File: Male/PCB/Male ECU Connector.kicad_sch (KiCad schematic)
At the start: 3 parts

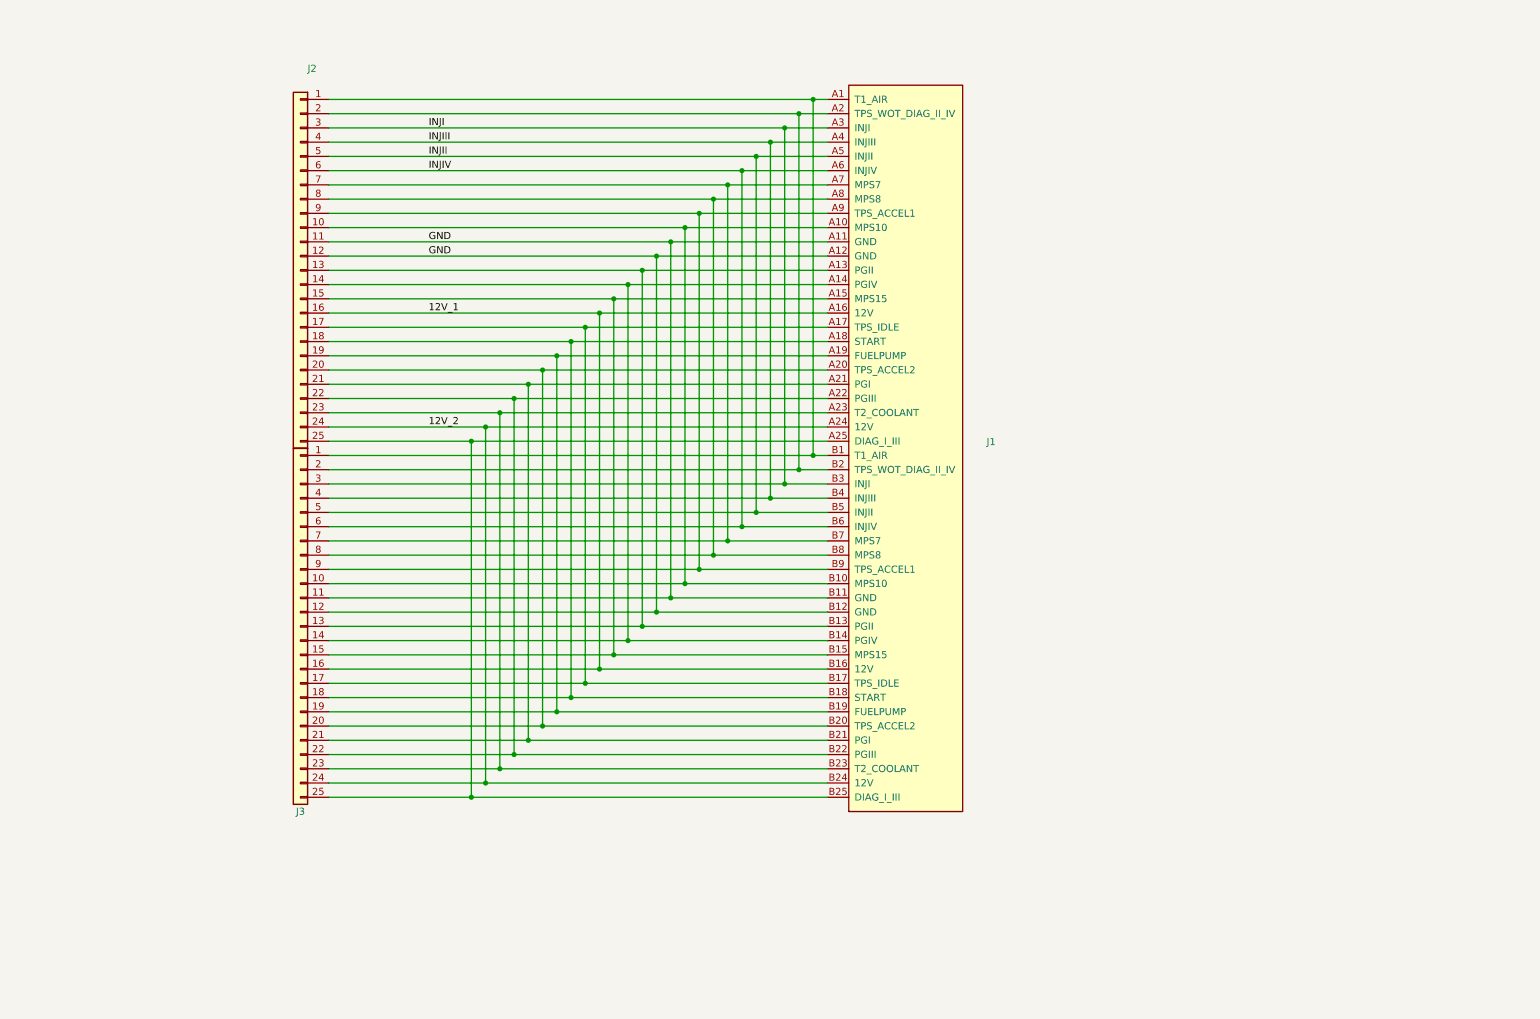
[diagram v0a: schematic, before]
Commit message: Added relay to disable fuel pump.
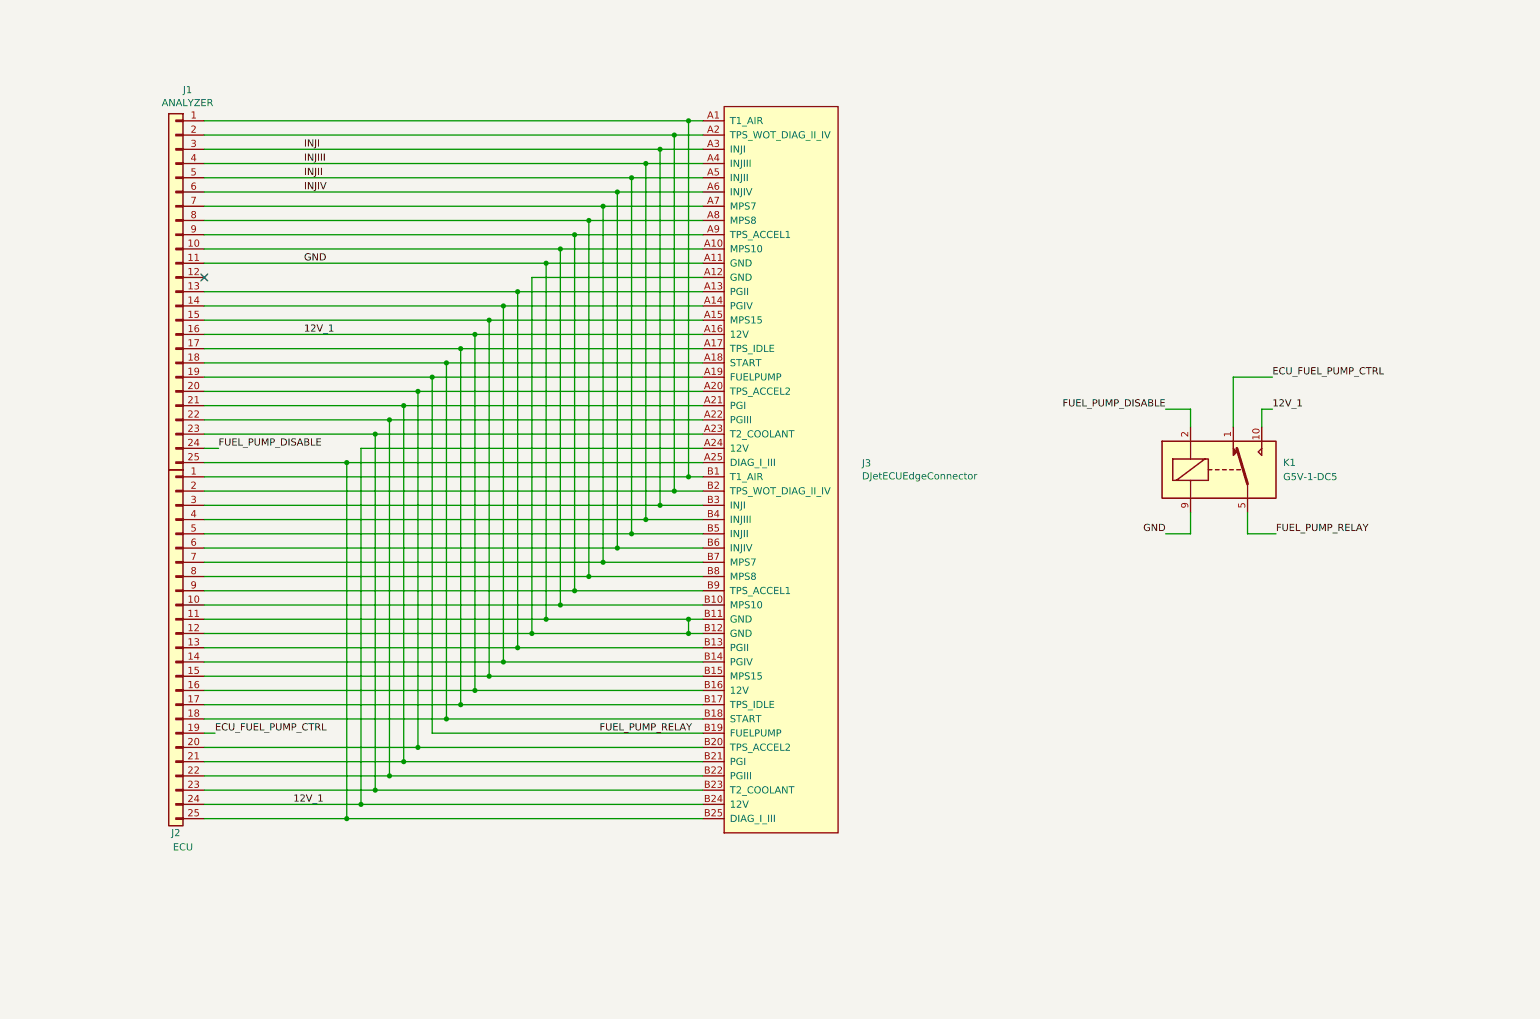
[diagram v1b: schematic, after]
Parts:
- added K1: G5V-1-DC5, Relay_THT:Relay_SPDT_Omron_G5V-1, symbol Relay:G5V-1
- J1: renamed from J2; value (none) -> ANALYZER; footprint (none) -> Connector_PinHeader_2.54mm:PinHeader_1x25_P2.54mm_Vertical
- J2: renamed from J3; value (none) -> ECU; footprint (none) -> Connector_PinHeader_2.54mm:PinHeader_1x25_P2.54mm_Vertical
- J3: renamed from J1; value (none) -> DJetECUEdgeConnector; footprint (none) -> Britishideas:D-Jetronic ECU Edge Connector
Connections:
- net 12V_1: now also J2.24 (Pin_24), J3.A24 (12V), J3.B24 (12V), K1.10
- net GND: now also K1.9; no longer J1.12 (Pin_12)
- net FUEL_PUMP_RELAY: now reaches J1.19 (Pin_19), J3.A19 (FUELPUMP), J3.B19 (FUELPUMP)
- net FUEL_PUMP_RELAY: now also K1.5, K1.6; no longer J2.19 (Pin_19)
- removed net 12V_2: J1.24 (Pin_24), J2.24 (Pin_24), J3.A24 (12V), J3.B24 (12V)
- new net ECU_FUEL_PUMP_CTRL: J2.19 (Pin_19), K1.1
- new net FUEL_PUMP_DISABLE: J1.24 (Pin_24), K1.2
- no-connect marks 0 -> 1
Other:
- moved on the sheet: J1, J2, J3

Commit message: Added larger holes for 18AWG (0.75mm2) engine harness wires. Rounded back corners of PCB to make it easier to design case. Added solder jumper to make relay optional.
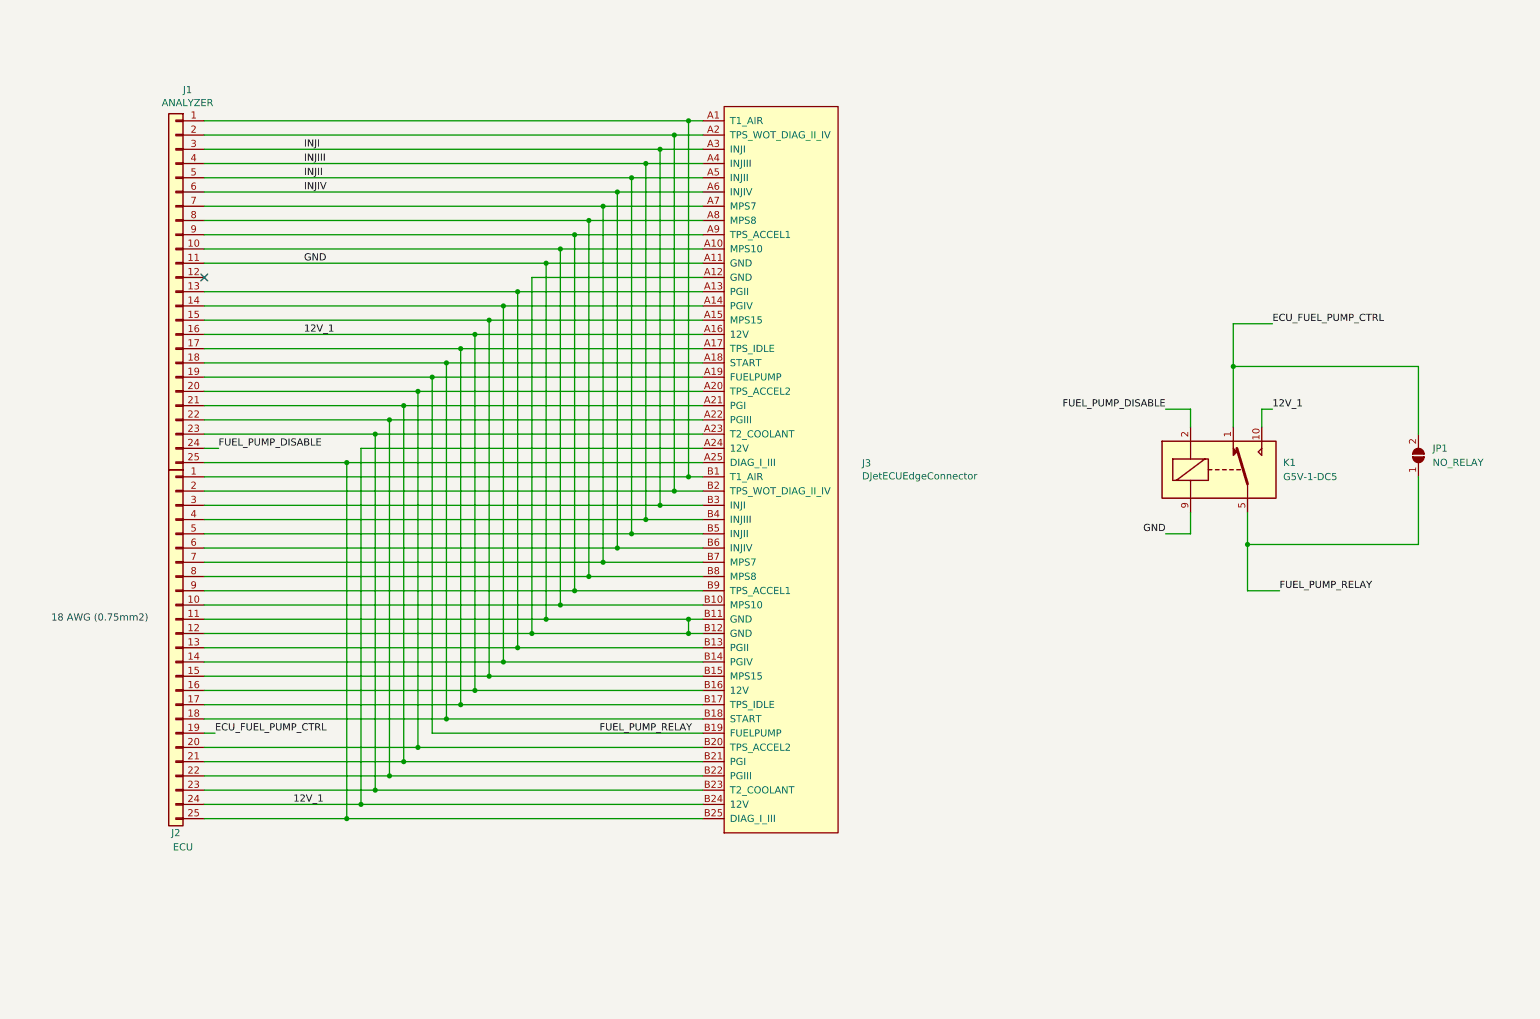
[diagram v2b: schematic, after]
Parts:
- added JP1: NO_RELAY, Jumper:SolderJumper-2_P1.3mm_Open_TrianglePad1.0x1.5mm, symbol Jumper:SolderJumper_2_Open
- J2: footprint Connector_PinHeader_2.54mm:PinHeader_1x25_P2.54mm_Vertical -> Britishideas:Pins_1x25_P3.00mm_18AWG
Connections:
- net ECU_FUEL_PUMP_CTRL: now also JP1.2 (B)
- net FUEL_PUMP_RELAY: now also JP1.1 (A)
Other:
- note added: "18 AWG (0.75mm2)"
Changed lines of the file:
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@@
   (title_block
     (title "Male ECU Connector for D-Jetronic")
-    (date "2023-10-20")
+    (date "2023-10-21")
     (rev "V1.1")
     (company "djetronic.org")
@@
   (junction (at 102.235 130.81) (diameter 0) (color 0 0 0 0)
   )
+  (junction (at 232.41 78.105) (diameter 0) (color 0 0 0 0)
+  )
   (junction (at 135.255 97.79) (diameter 0) (color 0 0 0 0)
   )
   (junction (at 97.155 135.89) (diameter 0) (color 0 0 0 0)
+  )
+  (junction (at 234.95 109.855) (diameter 0) (color 0 0 0 0)
   )
   (junction (at 109.855 59.69) (diameter 0) (color 0 0 0 0)
@@
     (stroke (width 0) (type default) (color 0 0 0 0))
   )
+  (wire (pts (xy 265.43 97.79) (xy 265.43 109.855))
+    (stroke (width 0) (type default) (color 0 0 0 0))
+  )
   (wire (pts (xy 48.895 118.11) (xy 114.935 118.11))
     (stroke (width 0) (type default) (color 0 0 0 0))
@@
     (stroke (width 0) (type default) (color 0 0 0 0))
   )
-  (wire (pts (xy 234.95 104.14) (xy 234.95 107.95))
+  (wire (pts (xy 234.95 104.14) (xy 234.95 109.855))
     (stroke (width 0) (type default) (color 0 0 0 0))
   )
@@
     (stroke (width 0) (type default) (color 0 0 0 0))
   )
+  (wire (pts (xy 265.43 78.105) (xy 232.41 78.105))
+    (stroke (width 0) (type default) (color 0 0 0 0))
+  )
   (wire (pts (xy 92.075 77.47) (xy 92.075 140.97))
     (stroke (width 0) (type default) (color 0 0 0 0))
   )
+  (wire (pts (xy 234.95 109.855) (xy 234.95 118.11))
+    (stroke (width 0) (type default) (color 0 0 0 0))
+  )
   (wire (pts (xy 97.155 72.39) (xy 97.155 135.89))
     (stroke (width 0) (type default) (color 0 0 0 0))
@@
     (stroke (width 0) (type default) (color 0 0 0 0))
   )
+  (wire (pts (xy 265.43 109.855) (xy 234.95 109.855))
+    (stroke (width 0) (type default) (color 0 0 0 0))
+  )
   (wire (pts (xy 102.235 67.31) (xy 102.235 130.81))
     (stroke (width 0) (type default) (color 0 0 0 0))
@@
     (stroke (width 0) (type default) (color 0 0 0 0))
   )
+  (wire (pts (xy 265.43 90.17) (xy 265.43 78.105))
+    (stroke (width 0) (type default) (color 0 0 0 0))
+  )
+  (wire (pts (xy 232.41 78.105) (xy 232.41 88.9))
+    (stroke (width 0) (type default) (color 0 0 0 0))
+  )
   (wire (pts (xy 48.895 52.07) (xy 117.475 52.07))
     (stroke (width 0) (type default) (color 0 0 0 0))
@@
     (stroke (width 0) (type default) (color 0 0 0 0))
   )
-  (wire (pts (xy 234.95 107.95) (xy 240.03 107.95))
+  (wire (pts (xy 234.95 118.11) (xy 240.665 118.11))
     (stroke (width 0) (type default) (color 0 0 0 0))
   )
@@
     (stroke (width 0) (type default) (color 0 0 0 0))
   )
-  (wire (pts (xy 232.41 80.01) (xy 232.41 88.9))
+  (wire (pts (xy 232.41 70.485) (xy 232.41 78.105))
     (stroke (width 0) (type default) (color 0 0 0 0))
   )
@@
     (stroke (width 0) (type default) (color 0 0 0 0))
   )
-  (wire (pts (xy 239.395 80.01) (xy 232.41 80.01))
+  (wire (pts (xy 239.395 70.485) (xy 232.41 70.485))
     (stroke (width 0) (type default) (color 0 0 0 0))
   )
@@
   (wire (pts (xy 48.895 133.35) (xy 99.695 133.35))
     (stroke (width 0) (type default) (color 0 0 0 0))
+  )
+  (text "18 AWG (0.75mm2)" (at 21.59 123.825 0)
+    (effects (font (size 1.27 1.27)) (justify left bottom))
   )
   (label "INJI" (at 66.675 39.37 0)
@@
     (effects (font (size 1.27 1.27)) (justify left bottom))
   )
-  (label "ECU_FUEL_PUMP_CTRL" (at 239.395 80.01 0)
+  (label "ECU_FUEL_PUMP_CTRL" (at 239.395 70.485 0)
     (effects (font (size 1.27 1.27)) (justify left bottom))
   )
@@
     (effects (font (size 1.27 1.27)) (justify left bottom))
   )
-  (label "FUEL_PUMP_RELAY" (at 240.03 107.95 0)
+  (label "FUEL_PUMP_RELAY" (at 240.665 118.11 0)
     (effects (font (size 1.27 1.27)) (justify left bottom))
   )
@@
     (property "Reference" "J2" (id 0) (at 43.815 161.29 0))
     (property "Value" "ECU" (id 1) (at 45.085 163.83 0))
-    (property "Footprint" "Connector_PinHeader_2.54mm:PinHeader_1x25_P2.54mm_Vertical" (id 2) (at 43.815 128.27 0)
+    (property "Footprint" "Britishideas:Pins_1x25_P3.00mm_18AWG" (id 2) (at 43.815 128.27 0)
       (effects (font (size 1.27 1.27)) hide)
     )
@@
     (pin "B9")
   )
+  (symbol (lib_id "Jumper:SolderJumper_2_Open") (at 265.43 93.98 90) (unit 1)
+    (in_bom yes) (on_board yes) (fields_autoplaced)
+    (property "Reference" "JP1" (id 0) (at 267.97 92.7099 90)
+      (effects (font (size 1.27 1.27)) (justify right))
+    )
+    (property "Value" "NO_RELAY" (id 1) (at 267.97 95.2499 90)
+      (effects (font (size 1.27 1.27)) (justify right))
+    )
+    (property "Footprint" "Jumper:SolderJumper-2_P1.3mm_Open_TrianglePad1.0x1.5mm" (id 2) (at 265.43 93.98 0)
+      (effects (font (size 1.27 1.27)) hide)
+    )
+    (property "Datasheet" "~" (id 3) (at 265.43 93.98 0)
+      (effects (font (size 1.27 1.27)) hide)
+    )
+    (pin "1")
+    (pin "2")
+  )
   (symbol (lib_id "Relay:G5V-1") (at 229.87 96.52 0) (unit 1)
     (in_bom yes) (on_board yes) (fields_autoplaced)
@@
     )
     (path "/00000000-0000-0000-0000-000063a4c84d"
-      (reference "J2") (unit 1) (value "ECU") (footprint "Connector_PinHeader_2.54mm:PinHeader_1x25_P2.54mm_Vertical")
+      (reference "J2") (unit 1) (value "ECU") (footprint "Britishideas:Pins_1x25_P3.00mm_18AWG")
     )
     (path "/00000000-0000-0000-0000-000063a83fd6"
       (reference "J3") (unit 1) (value "DJetECUEdgeConnector") (footprint "Britishideas:D-Jetronic ECU Edge Connector")
     )
+    (path "/55d5bbd5-2017-4585-9e31-4cd43e9a237c"
+      (reference "JP1") (unit 1) (value "NO_RELAY") (footprint "Jumper:SolderJumper-2_P1.3mm_Open_TrianglePad1.0x1.5mm")
+    )
     (path "/8cc33548-c40d-4c9c-80eb-e6492e7d188f"
